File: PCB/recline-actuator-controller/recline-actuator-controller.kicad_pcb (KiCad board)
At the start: 4 copper layers, 140 x 100 mm, 128 parts, among them J1 DX07S016JA1R1500, J10 1757242, J11 1757242, J12 0705530002, J13 0705530002, J14 0705530002, J15 0705530002, J2 Conn_01x03, J3 RJHSE-5381, J4 1757242, J5 1757242, J6 1757242, J7 1757242, J8 1757242, J9 1757242, M1 D24V22F5, M2 D24V22F3, Q1 PSMN7R0-60YS,115, Q2 PSMN7R0-60YS,115, Q3 PSMN7R0-60YS,115, Q4 PSMN7R0-60YS,115, Q5 PSMN7R0-60YS,115, Q6 BSC014N04LSIATMA1, Q7 BSC014N04LSIATMA1, SW1 TL3330AF260QG, SW2 TL3330AF260QG, U1 TEMPLATE, U2 RP2040, U3 MAX3535ECWI+T, U4 VNH5019ATR-E, U5 VNH5019ATR-E, X1 ABM8G-12.000MHZ-18-D2Y-T

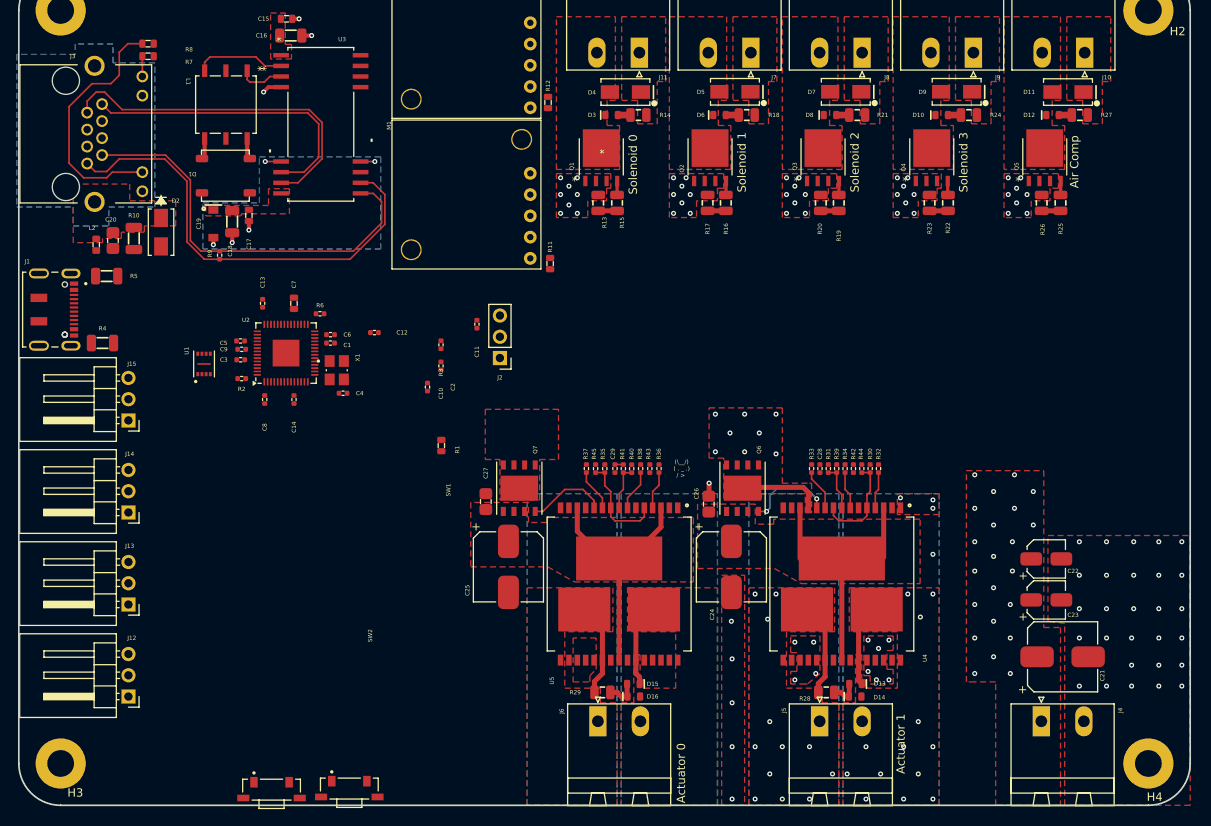
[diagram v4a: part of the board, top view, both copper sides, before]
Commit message: Actuator Control Board - RP2040
RP2040 section routed on Actuator control board !
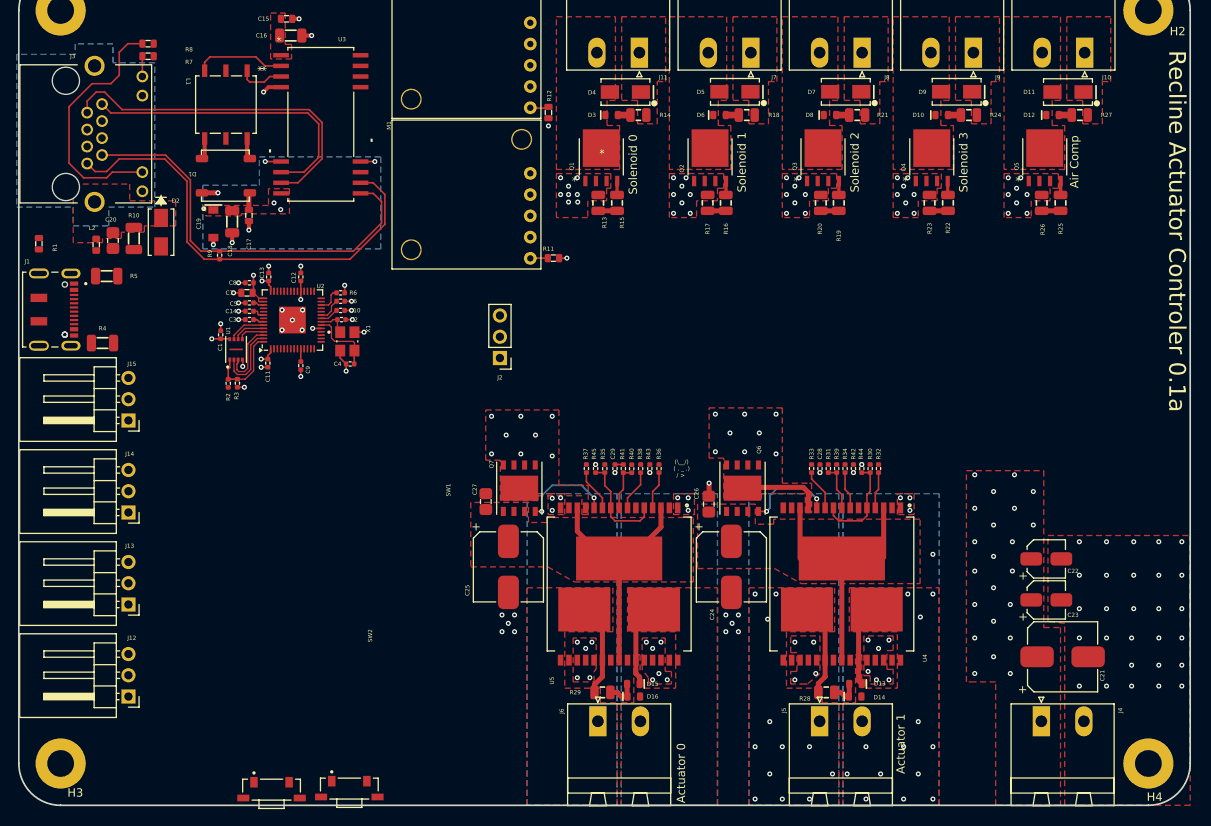
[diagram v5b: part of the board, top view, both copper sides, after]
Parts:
- moved R1 53.8 mm to (52.4, 77.9)
- moved C11 25.4 mm to (79.8, 92.2)
- moved R3 24.8 mm to (76.1, 94.5), turned to -90 degrees
- moved C8 14.1 mm to (77.6, 82.5), turned to 0 degrees
- moved C10 13.7 mm to (88.5, 85.8), turned to 180 degrees
- moved C1 13.2 mm to (74.1, 88.8), turned to -90 degrees
- moved C2 13.1 mm to (88.6, 87.0), turned to 180 degrees
- moved C14 11.8 mm to (77.6, 86.0), turned to 0 degrees
- moved C12 11.0 mm to (83.7, 81.8), turned to -90 degrees
- moved C9 7.33 mm to (83.7, 92.5), turned to 90 degrees
- moved C7 5.76 mm to (77.3, 83.8), turned to 0 degrees
- moved C3 4.91 mm to (77.6, 87.0)
- moved C5 4.67 mm to (77.6, 85.0)
- moved U1 4.20 mm to (76.0, 90.5)
- moved C6 4.18 mm to (88.5, 84.8)
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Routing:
- net +3.3V: track 0.00 -> 21.4 mm, vias 0 -> 11
- net GND: track 5.89 -> 22.4 mm, vias 87 -> 129
- net /RP2040/QSPI_SS: track 0.00 -> 10.1 mm
- net /RP2040/QSPI_SD1: track 0.00 -> 8.58 mm
- net Net-(U2-XIN): track 0.00 -> 8.17 mm
- net /RP2040/QSPI_SD2: track 0.00 -> 8.08 mm
- net +1V1: track 0.00 -> 5.59 mm
- net Net-(U2-XOUT): track 0.00 -> 4.54 mm
- net /RP2040/QSPI_SD3: track 0.00 -> 4.54 mm
- net /RP2040/QSPI_SCLK: track 0.00 -> 3.87 mm
- net /RP2040/QSPI_SD0: track 0.00 -> 3.21 mm
- net Net-(U2-RUN): track 0.00 -> 2.97 mm
- net /Power/3.3V_PG: track 0.00 -> 2.14 mm
- net /Power/5V_PG: track 0.00 -> 2.10 mm
- net +5V: track 0.00 -> 2.07 mm, vias 0 -> 2
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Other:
- board text added: "Recline Actuator Controler 0.1a"

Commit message: First Pass of PCB
First pass of PCB complete, needs review.
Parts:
- R4, R5: value RC1206FR-075K1L -> RC0402FR-075K1L; footprint AVR-KiCAD-Lib-Resistors:R1206 -> AVR-KiCAD-Lib-Resistors:R0402
- moved SW1 52.3 mm to (51.8, 99.3), turned to -90 degrees
- moved J15 51.6 mm to (103.0, 131.8), turned to -90 degrees
- moved SW2 51.0 mm to (51.9, 108.6), turned to -90 degrees
- moved J14 36.2 mm to (91.9, 131.8), turned to -90 degrees
- moved L2 26.4 mm to (68.7, 53.4), turned to 90 degrees
- moved D2 25.4 mm to (61.4, 51.7), turned to 90 degrees
- moved C20 25.4 mm to (66.7, 52.7), turned to 90 degrees
- moved R10 24.7 mm to (64.4, 52.6), turned to -90 degrees
- moved J13 20.8 mm to (80.9, 131.8), turned to -90 degrees
- moved J2 13.8 mm to (93.9, 89.0)
- moved J12 6.80 mm to (69.9, 131.8), turned to -90 degrees
- moved R7 3.84 mm to (67.8, 58.5)
- moved R8 3.84 mm to (67.8, 57.0)
- moved R5 2.82 mm to (58.8, 84.0)
- moved R4 2.50 mm to (58.9, 87.5)
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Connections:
- U2 pad 11: /RP2040/RS485_TXD -> /Motor H-Bridges/M1ENA/B
- U2 pad 12: /RP2040/RS485_RXD -> /Motor H-Bridges/M1INA
- U2 pad 13: /RP2040/RS485_TX_EN -> unconnected-(U2-GPIO10-Pad13)
- U2 pad 14: /RP2040/RS485_RX_EN -> /End Stop Limit Switches/MAX1
- U2 pad 15: /Motor H-Bridges/M1ENA/B -> /End Stop Limit Switches/MIN1
- U2 pad 16: /Motor H-Bridges/M1INA -> /End Stop Limit Switches/MAX2
- U2 pad 17: /Motor H-Bridges/M1INB -> /End Stop Limit Switches/MIN2
- U2 pad 18: /Motor H-Bridges/M1PWM -> unconnected-(U2-GPIO15-Pad18)
- U2 pad 2: /RP2040/AIR_COMP -> /Motor H-Bridges/M2INB
- U2 pad 27: /Motor H-Bridges/M1CS -> /RP2040/RS485_TXD
- U2 pad 28: /Motor H-Bridges/M2ENA/B -> /RP2040/RS485_RXD
- U2 pad 29: /Motor H-Bridges/M2INA -> /RP2040/RS485_TX_EN
- U2 pad 3: /RP2040/SOLENOID_0 -> /Motor H-Bridges/M2ENA/B
- U2 pad 30: /Motor H-Bridges/M2INB -> /RP2040/RS485_RX_EN
- U2 pad 31: /Motor H-Bridges/M2PWM -> /RP2040/RS485_RX_LED
- U2 pad 32: /Motor H-Bridges/M2CS -> /RP2040/RS485_TX_LED
- U2 pad 34: /End Stop Limit Switches/MAX1 -> /RP2040/AIR_COMP
- U2 pad 35: /End Stop Limit Switches/MIN1 -> /RP2040/SOLENOID_3
- U2 pad 36: /End Stop Limit Switches/MAX2 -> /RP2040/SOLENOID_2
- U2 pad 37: /End Stop Limit Switches/MIN2 -> /RP2040/SOLENOID_1
- U2 pad 38: /Power/5V_PG -> /RP2040/SOLENOID_0
- U2 pad 39: /Power/3.3V_PG -> /Power/5V_PG
- U2 pad 4: /RP2040/SOLENOID_1 -> /Motor H-Bridges/M2CS
- U2 pad 40: unconnected-(U2-GPIO28_ADC2-Pad40) -> /Power/3.3V_PG
- U2 pad 5: /RP2040/SOLENOID_2 -> /Motor H-Bridges/M2PWM
- U2 pad 6: /RP2040/SOLENOID_3 -> /Motor H-Bridges/M2INA
- U2 pad 7: unconnected-(U2-GPIO5-Pad7) -> /Motor H-Bridges/M1INB
- U2 pad 8: /RP2040/RS485_RX_LED -> /Motor H-Bridges/M1CS
- U2 pad 9: /RP2040/RS485_TX_LED -> /Motor H-Bridges/M1PWM
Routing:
- net /RP2040/AIR_COMP: track 2.25 -> 100.3 mm, vias 0 -> 2
- net /RP2040/SOLENOID_3: track 2.20 -> 87.4 mm, vias 0 -> 2
- net /Motor H-Bridges/M1PWM: track 0.00 -> 81.0 mm
- net /Motor H-Bridges/M1INA: track 0.00 -> 80.5 mm
- net /Motor H-Bridges/M1ENA/B: track 0.00 -> 80.1 mm
- net /Motor H-Bridges/M1CS: track 0.00 -> 78.7 mm
- net /Motor H-Bridges/M1INB: track 0.00 -> 77.4 mm
- net /RP2040/SOLENOID_2: track 2.15 -> 75.2 mm, vias 0 -> 2
- net /RP2040/RS485_TX_LED: track 0.00 -> 63.6 mm
- net /RP2040/RS485_RX_LED: track 0.00 -> 63.5 mm
- net /RP2040/SOLENOID_1: track 2.18 -> 63.4 mm, vias 0 -> 2
- net /Motor H-Bridges/M2INA: track 0.00 -> 57.5 mm
- net /Motor H-Bridges/M2PWM: track 0.00 -> 56.9 mm
- net /End Stop Limit Switches/MIN2: track 0.00 -> 56.7 mm, vias 0 -> 1
- net /Motor H-Bridges/M2CS: track 1.00 -> 55.0 mm
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- added copper zone on F.Cu, net Net-(J1-SHIELD-PadS1)
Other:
- board text removed: "(\__/) ( . _ .) / >"

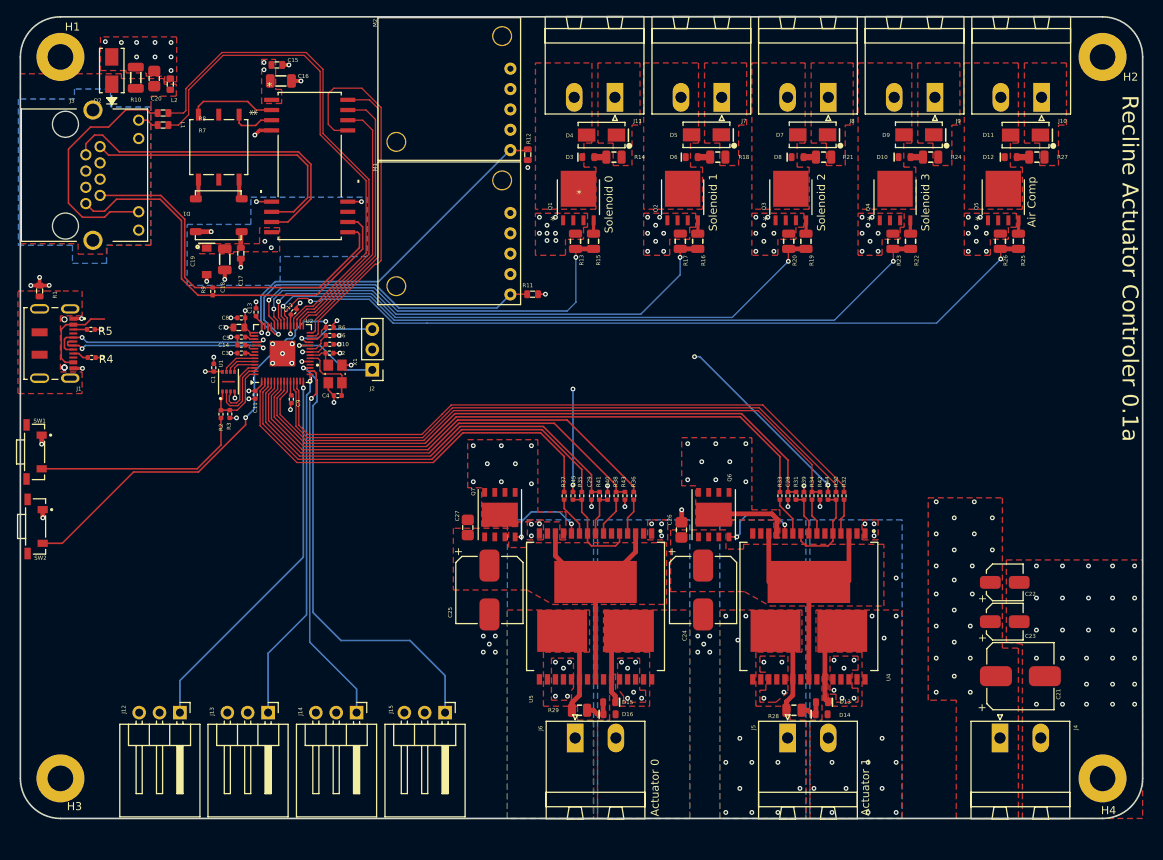
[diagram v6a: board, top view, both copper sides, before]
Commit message: All Hardware Tweaked / 3D Renders
PCBs for Actuator Control, Recline Control HID, and 7 Segment carrier are all complete with full 3D models rendering. 3D Renders of all board added to repository img directory.
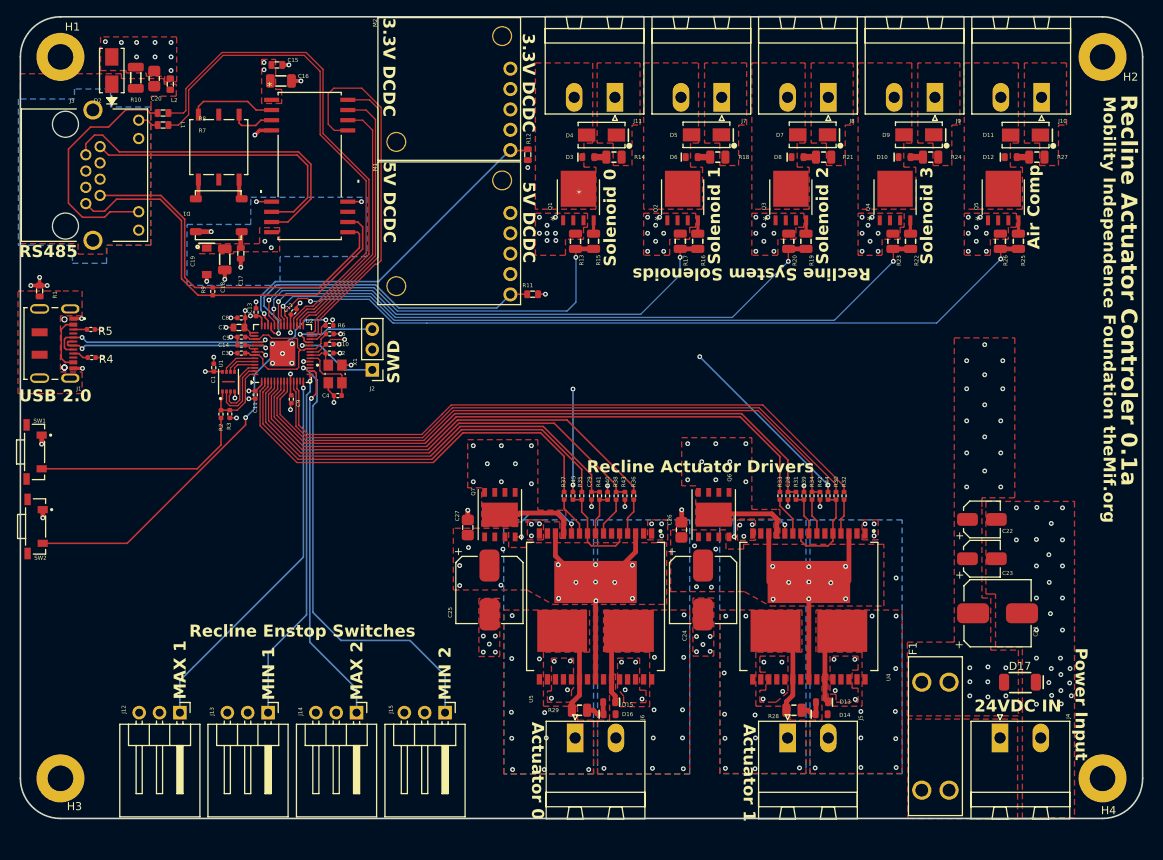
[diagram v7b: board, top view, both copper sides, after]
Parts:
- added D17: SMAJ24A, AVR-KiCAD-Lib-Diodes:SMAJ, F.Cu at (174.7, 128.0)
- added F1: 3557-2, AVR-KiCAD-Lib-Fuse-Holders:FUSE_3557-2, F.Cu at (164.2, 134.7)
- D11, D4, D5, D7, D9: value B240A-13-F -> SMA
- D2: value SMAJ30CA -> SMASeries
- moved C23 8.35 mm to (169.9, 112.6)
- moved C22 8.35 mm to (169.9, 107.7)
- moved C21 8.35 mm to (171.9, 119.4)
- moved R6 0.25 mm to (88.5, 83.5)
- moved C6 0.20 mm to (88.6, 84.5)
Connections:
- J4 pad 1: +24V -> Net-(F1-Pad2)
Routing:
- net +1V1: track 5.64 -> 23.3 mm
- net +24V: track 10.0 -> 20.1 mm, vias 38 -> 39
- net VBUS: track 11.2 -> 7.06 mm
- net +3.3V: track 60.4 -> 63.8 mm, vias 16 -> 18
- net /Power/3.3V_PG: track 46.9 -> 44.9 mm
- net GND: track 37.0 -> 37.8 mm, vias 148 -> 144
- net Net-(J2-Pin_1): track 11.7 -> 11.0 mm
- net Net-(U2-USB_DP): track 27.1 -> 27.7 mm
- net Net-(Q6-G): track 10.7 -> 11.3 mm
- net Net-(J2-Pin_3): track 10.5 -> 11.1 mm
- net Net-(U2-USB_DM): track 28.7 -> 29.2 mm
- net /Motor H-Bridges/M2OUTA: vias 3 -> 13
- net /Motor H-Bridges/VMOT2: vias 0 -> 14
- net /Motor H-Bridges/VMOT1: vias 0 -> 13
- net /Motor H-Bridges/M2OUTB: vias 3 -> 13
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- added copper zone on In2.Cu, net /Motor H-Bridges/VMOT1
- added copper zone on In2.Cu, net /Motor H-Bridges/VMOT2
- added copper zone on In2.Cu, net GND
- added copper zone on F.Cu, net Net-(F1-Pad2)
- added copper zone on In2.Cu, net Net-(F1-Pad2)
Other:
- board text added: "24V"
- board text added: "24V Rail"
- board text added: "24VDC IN"
- board text added: "3.3V DCDC"
- board text added: "3V3"
- board text added: "3V3 PG"
- board text added: "3V3 Rail"
- board text added: "5V DCDC"
- board text added: "5V PG"
- board text added: "5V Rail"
- board text added: "Accessibilita Project"
- board text added: "Designed by Adam Vadala-Roth"
- board text added: "GND"
- board text added: "GhostPCB LLC"
- board text added: "M1OUTA"
- board text added: "M1OUTB"
- board text added: "M2OUTA"
- board text added: "M2OUTB"
- board text added: "MAX 1"
- board text added: "MAX 2"
- board text added: "MAX1"
- board text added: "MAX2"
- board text added: "MIN 1"
- board text added: "MIN 2"
- board text added: "MIN1"
- board text added: "MIN2"
- board text added: "Mobility Independence Foundation"
- board text added: "Mobility Independence Foundation theMif.org"
- board text added: "Power Input"
- board text added: "RS485"
- board text added: "Recline Actuator Controller 0.1a 2024"
- board text added: "Recline Actuator Drivers"
- board text added: "Recline Enstop Switches"
- board text added: "Recline System Solenoids"
- board text added: "SWCLK"
- board text added: "SWD"
- board text added: "USB 2.0"
- board text added: "https://github.com/Accessibilita"
